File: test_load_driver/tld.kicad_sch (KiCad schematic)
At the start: 6 parts, among them J1 input, J2 power, J3 output, Q1 IRFZ44N, U1 TC427

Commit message: added debouncing capacitor
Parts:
- added C1: 100nF, Capacitor_THT:C_Rect_L9.0mm_W2.5mm_P7.50mm_MKT, symbol Device:C
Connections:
- net GND: now also C1.2
- net at F1.1, J3.1 (Pin_1), U1.6 (V+): now also C1.1
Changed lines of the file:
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@@
 (kicad_sch (version 20230121) (generator eeschema)
   (paper "A4")
+  (junction (at 88.9 76.2) (diameter 0) (color 0 0 0 0)
+  )
   (junction (at 101.6 76.2) (diameter 0) (color 0 0 0 0)
   )
@@
     (stroke (width 0) (type default))
   )
-  (wire (pts (xy 101.6 76.2) (xy 74.93 76.2))
+  (wire (pts (xy 101.6 76.2) (xy 88.9 76.2))
+    (stroke (width 0) (type default))
+  )
+  (wire (pts (xy 88.9 85.09) (xy 88.9 83.82))
     (stroke (width 0) (type default))
   )
@@
   )
   (wire (pts (xy 95.25 60.96) (xy 101.6 60.96))
+    (stroke (width 0) (type default))
+  )
+  (wire (pts (xy 88.9 76.2) (xy 74.93 76.2))
     (stroke (width 0) (type default))
   )
@@
     )
   )
+  (symbol (lib_id "power:GND") (at 88.9 85.09 0) (mirror y) (unit 1)
+    (in_bom yes) (on_board yes) (dnp no)
+    (property "Reference" "#PWR01" (at 88.9 91.44 0)
+      (effects (font (size 1.27 1.27)) hide)
+    )
+    (property "Value" "GND" (at 88.9 90.17 0)
+      (effects (font (size 1.27 1.27)))
+    )
+    (property "Footprint" "" (at 88.9 85.09 0)
+      (effects (font (size 1.27 1.27)) hide)
+    )
+    (property "Datasheet" "" (at 88.9 85.09 0)
+      (effects (font (size 1.27 1.27)) hide)
+    )
+    (pin "1")
+    (instances
+      (project "tld"
+        (path "/a10465dc-4832-4429-a9e9-d3c861172a8d"
+          (reference "#PWR01") (unit 1)
+        )
+      )
+    )
+  )
   (symbol (lib_id "Connector:Screw_Terminal_01x02") (at 106.68 86.36 0) (unit 1)
     (in_bom yes) (on_board yes) (dnp no) (fields_autoplaced)
@@
         )
       )
+    )
+  )
+  (symbol (lib_id "Device:C") (at 88.9 80.01 0) (unit 1)
+    (in_bom yes) (on_board yes) (dnp no) (fields_autoplaced)
+    (property "Reference" "C1" (at 92.71 78.74 0)
+      (effects (font (size 1.27 1.27)) (justify left))
+    )
+    (property "Value" "100nF" (at 92.71 81.28 0)
+      (effects (font (size 1.27 1.27)) (justify left))
+    )
+    (property "Footprint" "Capacitor_THT:C_Rect_L9.0mm_W2.5mm_P7.50mm_MKT" (at 89.8652 83.82 0)
+      (effects (font (size 1.27 1.27)) hide)
+    )
+    (property "Datasheet" "~" (at 88.9 80.01 0)
+      (effects (font (size 1.27 1.27)) hide)
+    )
+    (pin "2")
+    (pin "1")
+    (instances
+      (project "tld"
+        (path "/a10465dc-4832-4429-a9e9-d3c861172a8d"
+          (reference "C1") (unit 1)
+        )
+      )

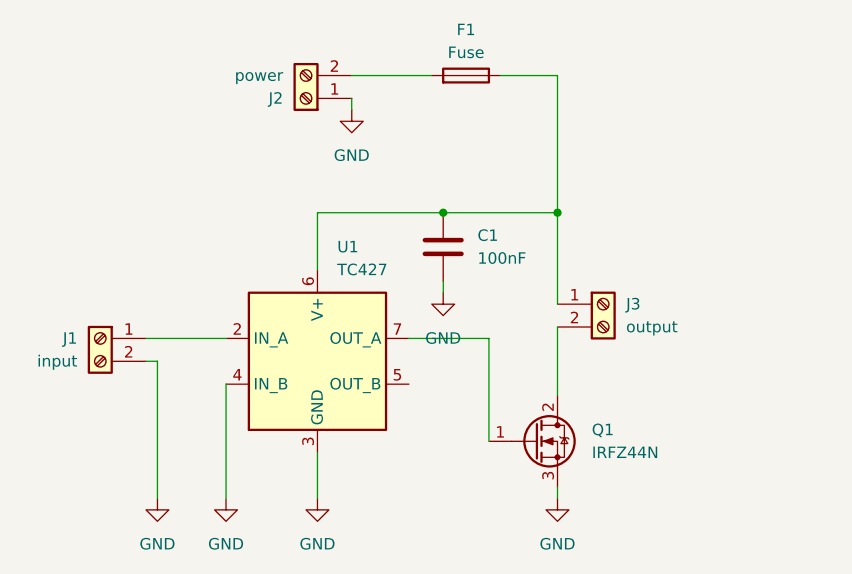
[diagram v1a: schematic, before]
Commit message: added 1N4001 diode to protect the transistor
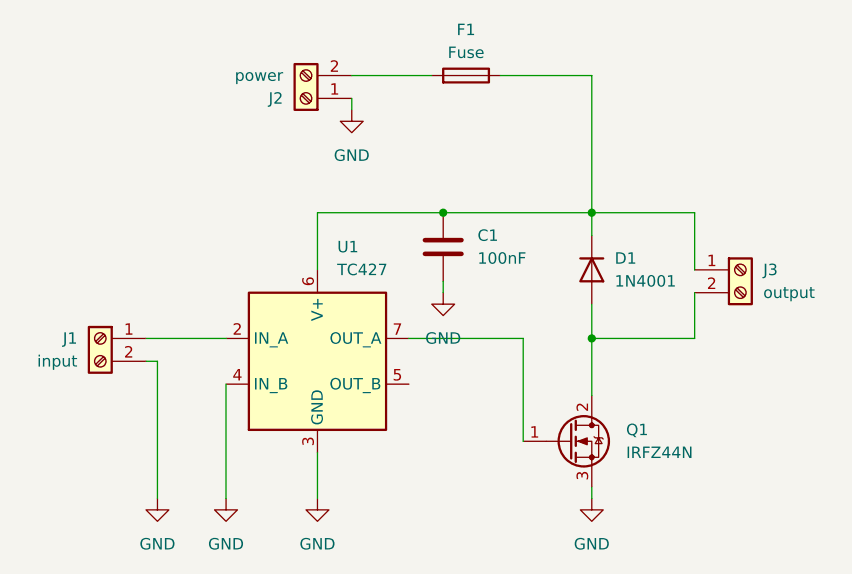
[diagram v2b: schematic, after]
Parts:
- added D1: 1N4001, Diode_THT:D_DO-41_SOD81_P10.16mm_Horizontal, symbol Diode:1N4001
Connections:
- net at C1.1, F1.1, J3.1 (Pin_1)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: now also D1.1 (K)
- net at J3.2 (Pin_2), Q1.2 (D): now also D1.2 (A)
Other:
- moved on the sheet: J3, Q1
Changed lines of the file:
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@@
   (junction (at 88.9 76.2) (diameter 0) (color 0 0 0 0)
   )
-  (junction (at 101.6 76.2) (diameter 0) (color 0 0 0 0)
-  )
-  (wire (pts (xy 101.6 76.2) (xy 101.6 86.36))
-    (stroke (width 0) (type default))
-  )
-  (wire (pts (xy 101.6 60.96) (xy 101.6 76.2))
+  (junction (at 105.41 76.2) (diameter 0) (color 0 0 0 0)
+  )
+  (junction (at 105.41 90.17) (diameter 0) (color 0 0 0 0)
+  )
+  (wire (pts (xy 116.84 76.2) (xy 116.84 82.55))
+    (stroke (width 0) (type default))
+  )
+  (wire (pts (xy 105.41 60.96) (xy 105.41 76.2))
+    (stroke (width 0) (type default))
+  )
+  (wire (pts (xy 88.9 76.2) (xy 105.41 76.2))
     (stroke (width 0) (type default))
   )
@@
     (stroke (width 0) (type default))
   )
-  (wire (pts (xy 101.6 76.2) (xy 88.9 76.2))
-    (stroke (width 0) (type default))
-  )
   (wire (pts (xy 88.9 85.09) (xy 88.9 83.82))
     (stroke (width 0) (type default))
   )
+  (wire (pts (xy 116.84 76.2) (xy 105.41 76.2))
+    (stroke (width 0) (type default))
+  )
+  (wire (pts (xy 105.41 90.17) (xy 105.41 96.52))
+    (stroke (width 0) (type default))
+  )
   (wire (pts (xy 74.93 107.95) (xy 74.93 102.87))
     (stroke (width 0) (type default))
@@
     (stroke (width 0) (type default))
   )
-  (wire (pts (xy 85.09 90.17) (xy 93.98 90.17))
-    (stroke (width 0) (type default))
-  )
-  (wire (pts (xy 93.98 90.17) (xy 93.98 101.6))
+  (wire (pts (xy 85.09 90.17) (xy 97.79 90.17))
+    (stroke (width 0) (type default))
+  )
+  (wire (pts (xy 97.79 90.17) (xy 97.79 101.6))
     (stroke (width 0) (type default))
   )
@@
     (stroke (width 0) (type default))
   )
-  (wire (pts (xy 101.6 107.95) (xy 101.6 106.68))
-    (stroke (width 0) (type default))
-  )
-  (wire (pts (xy 101.6 96.52) (xy 101.6 88.9))
+  (wire (pts (xy 105.41 107.95) (xy 105.41 106.68))
+    (stroke (width 0) (type default))
+  )
+  (wire (pts (xy 116.84 90.17) (xy 116.84 85.09))
+    (stroke (width 0) (type default))
+  )
+  (wire (pts (xy 116.84 90.17) (xy 105.41 90.17))
     (stroke (width 0) (type default))
   )
@@
     (stroke (width 0) (type default))
   )
+  (wire (pts (xy 105.41 86.36) (xy 105.41 90.17))
+    (stroke (width 0) (type default))
+  )
+  (wire (pts (xy 105.41 76.2) (xy 105.41 78.74))
+    (stroke (width 0) (type default))
+  )
   (wire (pts (xy 64.77 107.95) (xy 64.77 95.25))
     (stroke (width 0) (type default))
   )
-  (wire (pts (xy 95.25 60.96) (xy 101.6 60.96))
+  (wire (pts (xy 95.25 60.96) (xy 105.41 60.96))
     (stroke (width 0) (type default))
   )
@@
     )
   )
-  (symbol (lib_id "Connector:Screw_Terminal_01x02") (at 106.68 86.36 0) (unit 1)
-    (in_bom yes) (on_board yes) (dnp no) (fields_autoplaced)
-    (property "Reference" "J3" (at 109.22 86.36 0)
-      (effects (font (size 1.27 1.27)) (justify left))
-    )
-    (property "Value" "output" (at 109.22 88.9 0)
-      (effects (font (size 1.27 1.27)) (justify left))
-    )
-    (property "Footprint" "Connector_PinHeader_2.54mm:PinHeader_1x02_P2.54mm_Vertical" (at 106.68 86.36 0)
-      (effects (font (size 1.27 1.27)) hide)
-    )
-    (property "Datasheet" "~" (at 106.68 86.36 0)
+  (symbol (lib_id "Connector:Screw_Terminal_01x02") (at 121.92 82.55 0) (unit 1)
+    (in_bom yes) (on_board yes) (dnp no) (fields_autoplaced)
+    (property "Reference" "J3" (at 124.46 82.55 0)
+      (effects (font (size 1.27 1.27)) (justify left))
+    )
+    (property "Value" "output" (at 124.46 85.09 0)
+      (effects (font (size 1.27 1.27)) (justify left))
+    )
+    (property "Footprint" "Connector_PinHeader_2.54mm:PinHeader_1x02_P2.54mm_Vertical" (at 121.92 82.55 0)
+      (effects (font (size 1.27 1.27)) hide)
+    )
+    (property "Datasheet" "~" (at 121.92 82.55 0)
       (effects (font (size 1.27 1.27)) hide)
     )
@@
     )
   )
-  (symbol (lib_id "Transistor_FET:BUZ11") (at 99.06 101.6 0) (unit 1)
-    (in_bom yes) (on_board yes) (dnp no) (fields_autoplaced)
-    (property "Reference" "Q1" (at 105.41 100.33 0)
-      (effects (font (size 1.27 1.27)) (justify left))
-    )
-    (property "Value" "IRFZ44N" (at 105.41 102.87 0)
-      (effects (font (size 1.27 1.27)) (justify left))
-    )
-    (property "Footprint" "Package_TO_SOT_THT:TO-220-3_Vertical" (at 104.14 103.505 0)
+  (symbol (lib_id "Transistor_FET:BUZ11") (at 102.87 101.6 0) (unit 1)
+    (in_bom yes) (on_board yes) (dnp no) (fields_autoplaced)
+    (property "Reference" "Q1" (at 109.22 100.33 0)
+      (effects (font (size 1.27 1.27)) (justify left))
+    )
+    (property "Value" "IRFZ44N" (at 109.22 102.87 0)
+      (effects (font (size 1.27 1.27)) (justify left))
+    )
+    (property "Footprint" "Package_TO_SOT_THT:TO-220-3_Vertical" (at 107.95 103.505 0)
       (effects (font (size 1.27 1.27) italic) (justify left) hide)
     )
-    (property "Datasheet" "https://media.digikey.com/pdf/Data%20Sheets/Fairchild%20PDFs/BUZ11.pdf" (at 104.14 105.41 0)
+    (property "Datasheet" "https://media.digikey.com/pdf/Data%20Sheets/Fairchild%20PDFs/BUZ11.pdf" (at 107.95 105.41 0)
       (effects (font (size 1.27 1.27)) (justify left) hide)
     )
@@
     )
   )
-  (symbol (lib_id "power:GND") (at 101.6 107.95 0) (mirror y) (unit 1)
-    (in_bom yes) (on_board yes) (dnp no) (fields_autoplaced)
-    (property "Reference" "#PWR06" (at 101.6 114.3 0)
-      (effects (font (size 1.27 1.27)) hide)
-    )
-    (property "Value" "GND" (at 101.6 113.03 0)
+  (symbol (lib_id "power:GND") (at 105.41 107.95 0) (mirror y) (unit 1)
+    (in_bom yes) (on_board yes) (dnp no) (fields_autoplaced)
+    (property "Reference" "#PWR06" (at 105.41 114.3 0)
+      (effects (font (size 1.27 1.27)) hide)
+    )
+    (property "Value" "GND" (at 105.41 113.03 0)
       (effects (font (size 1.27 1.27)))
     )
-    (property "Footprint" "" (at 101.6 107.95 0)
-      (effects (font (size 1.27 1.27)) hide)
-    )
-    (property "Datasheet" "" (at 101.6 107.95 0)
+    (property "Footprint" "" (at 105.41 107.95 0)
+      (effects (font (size 1.27 1.27)) hide)
+    )
+    (property "Datasheet" "" (at 105.41 107.95 0)
       (effects (font (size 1.27 1.27)) hide)
     )
@@
         )
       )
+    )
+  )
+  (symbol (lib_id "Diode:1N4001") (at 105.41 82.55 270) (unit 1)
+    (in_bom yes) (on_board yes) (dnp no) (fields_autoplaced)
+    (property "Reference" "D1" (at 107.95 81.28 90)
+      (effects (font (size 1.27 1.27)) (justify left))
+    )
+    (property "Value" "1N4001" (at 107.95 83.82 90)
+      (effects (font (size 1.27 1.27)) (justify left))
+    )
+    (property "Footprint" "Diode_THT:D_DO-41_SOD81_P10.16mm_Horizontal" (at 105.41 82.55 0)
+      (effects (font (size 1.27 1.27)) hide)
+    )
+    (property "Datasheet" "http://www.vishay.com/docs/88503/1n4001.pdf" (at 105.41 82.55 0)
+      (effects (font (size 1.27 1.27)) hide)
+    )
+    (property "Sim.Device" "D" (at 105.41 82.55 0)
+      (effects (font (size 1.27 1.27)) hide)
+    )
+    (property "Sim.Pins" "1=K 2=A" (at 105.41 82.55 0)
+      (effects (font (size 1.27 1.27)) hide)
+    )
+    (pin "1")
+    (pin "2")
+    (instances
+      (project "tld"
+        (path "/a10465dc-4832-4429-a9e9-d3c861172a8d"
+          (reference "D1") (unit 1)
+        )
+      )

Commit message: non-inverting version
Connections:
- net GND: no longer U1.4 (IN_B)
- net at J1.1 (Pin_1): now also U1.4 (IN_B); no longer U1.2 (IN_A)
- net at U1.5 (OUT_B): now also U1.2 (IN_A)
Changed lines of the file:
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@@
+    (stroke (width 0) (type default))
+  )
+  (wire (pts (xy 60.96 90.17) (xy 55.88 90.17))
     (stroke (width 0) (type default))
   )
@@
     (stroke (width 0) (type default))
   )
-  (wire (pts (xy 55.88 90.17) (xy 64.77 90.17))
-    (stroke (width 0) (type default))
-  )
   (wire (pts (xy 88.9 85.09) (xy 88.9 83.82))
     (stroke (width 0) (type default))
@@
     (stroke (width 0) (type default))
   )
+  (wire (pts (xy 63.5 72.39) (xy 63.5 90.17))
+    (stroke (width 0) (type default))
+  )
+  (wire (pts (xy 86.36 72.39) (xy 63.5 72.39))
+    (stroke (width 0) (type default))
+  )
+  (wire (pts (xy 86.36 95.25) (xy 86.36 72.39))
+    (stroke (width 0) (type default))
+  )
   (wire (pts (xy 74.93 76.2) (xy 74.93 82.55))
     (stroke (width 0) (type default))
   )
+  (wire (pts (xy 63.5 90.17) (xy 64.77 90.17))
+    (stroke (width 0) (type default))
+  )
   (wire (pts (xy 85.09 90.17) (xy 97.79 90.17))
     (stroke (width 0) (type default))
@@
     (stroke (width 0) (type default))
   )
+  (wire (pts (xy 60.96 95.25) (xy 60.96 90.17))
+    (stroke (width 0) (type default))
+  )
   (wire (pts (xy 116.84 90.17) (xy 105.41 90.17))
     (stroke (width 0) (type default))
@@
     (stroke (width 0) (type default))
   )
+  (wire (pts (xy 85.09 95.25) (xy 86.36 95.25))
+    (stroke (width 0) (type default))
+  )
   (wire (pts (xy 105.41 86.36) (xy 105.41 90.17))
     (stroke (width 0) (type default))
@@
     (stroke (width 0) (type default))
   )
-  (wire (pts (xy 64.77 107.95) (xy 64.77 95.25))
+  (wire (pts (xy 64.77 95.25) (xy 60.96 95.25))
     (stroke (width 0) (type default))
   )
@@
       (effects (font (size 1.27 1.27)) hide)
     )
-    (property "Value" "GND" (at 88.9 90.17 0)
+    (property "Value" "GND" (at 92.71 86.36 0)
       (effects (font (size 1.27 1.27)))
     )
@@
         )
       )
-    )
-  )
-  (symbol (lib_id "power:GND") (at 64.77 107.95 0) (mirror y) (unit 1)
-    (in_bom yes) (on_board yes) (dnp no)
-    (property "Reference" "#PWR05" (at 64.77 114.3 0)
-      (effects (font (size 1.27 1.27)) hide)
-    )
-    (property "Value" "GND" (at 64.77 113.03 0)
-      (effects (font (size 1.27 1.27)))
-    )
-    (property "Footprint" "" (at 64.77 107.95 0)
-      (effects (font (size 1.27 1.27)) hide)
-    )
-    (property "Datasheet" "" (at 64.77 107.95 0)
-      (effects (font (size 1.27 1.27)) hide)
-    )
-    (pin "1")
-    (instances
-      (project "tld"
-        (path "/a10465dc-4832-4429-a9e9-d3c861172a8d"
-          (reference "#PWR05") (unit 1)
-        )
-      )
